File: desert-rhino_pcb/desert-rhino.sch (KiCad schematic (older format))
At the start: 0 parts

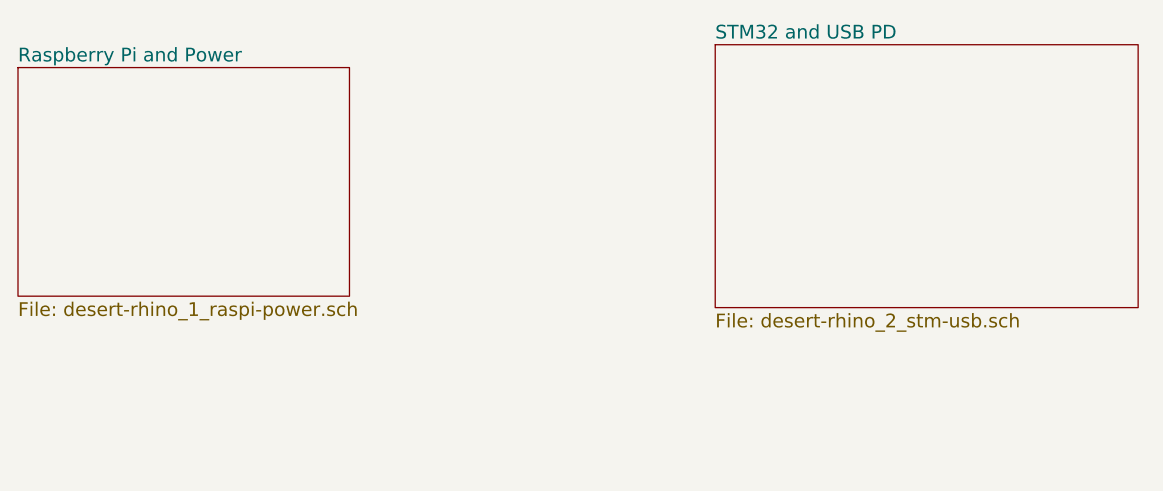
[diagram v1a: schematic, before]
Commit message: Finished most of schem. Still need ina230
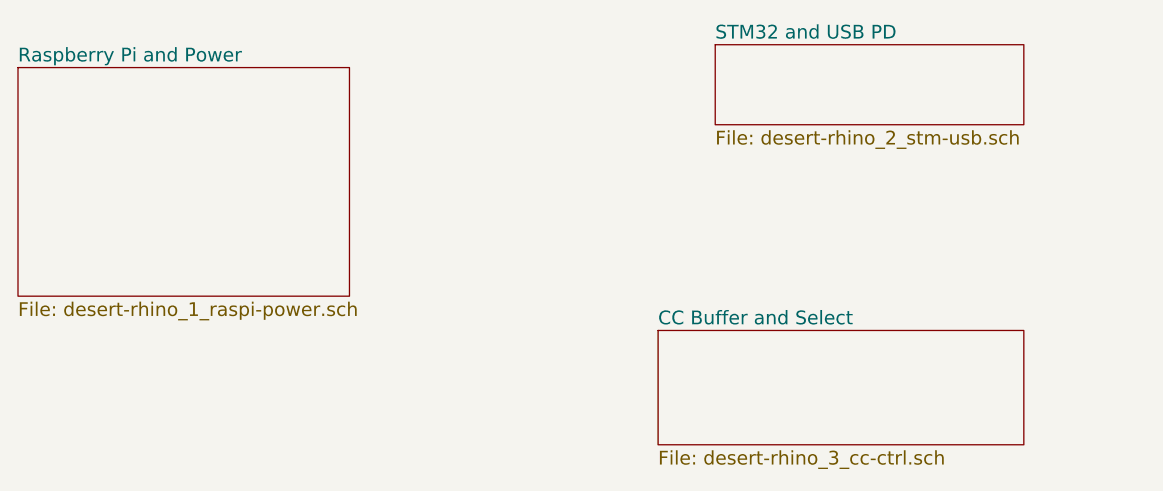
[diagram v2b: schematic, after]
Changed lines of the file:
@@
 $Descr A4 11693 8268
 encoding utf-8
-Sheet 1 3
+Sheet 1 4
 Title ""
 Date ""
@@
 $EndSheet
 $Sheet
-S 5300 1800 1850 1150
+S 5300 1800 1350 350
 U 5A6034DD
 F0 "STM32 and USB PD" 60
 F1 "desert-rhino_2_stm-usb.sch" 60
 $EndSheet
+$Sheet
+S 5050 3050 1600 500
+U 5A687A1F
+F0 "CC Buffer and Select" 60
+F1 "desert-rhino_3_cc-ctrl.sch" 60
+$EndSheet
 $EndSCHEMATC
